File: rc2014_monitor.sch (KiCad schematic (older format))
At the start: 28 parts, among them J1 Z80 Bus, J2 Pro Bus, J3 USB_B_Micro, J4 M3 Mounting Hole, SW2 SW_Push, U1 74HCT541, U11 74HCT00, U2 74HCT541, U3 74HCT541, U7 MAX40200AUK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

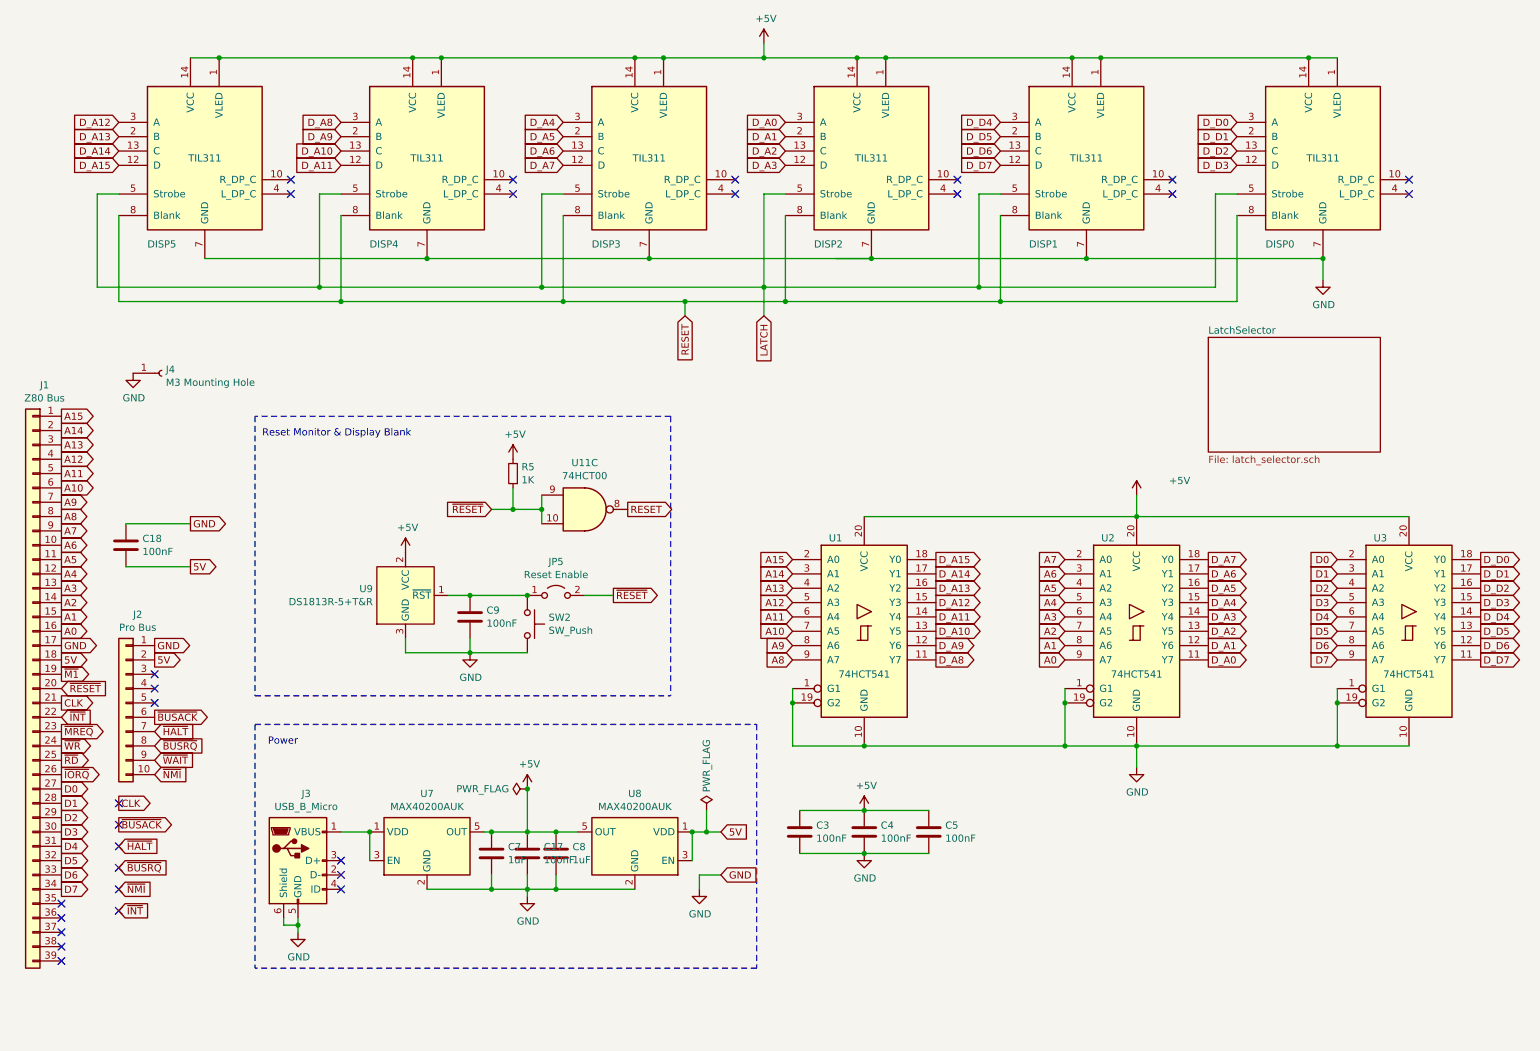
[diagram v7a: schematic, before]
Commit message: added extra filter cap, opened groundplane
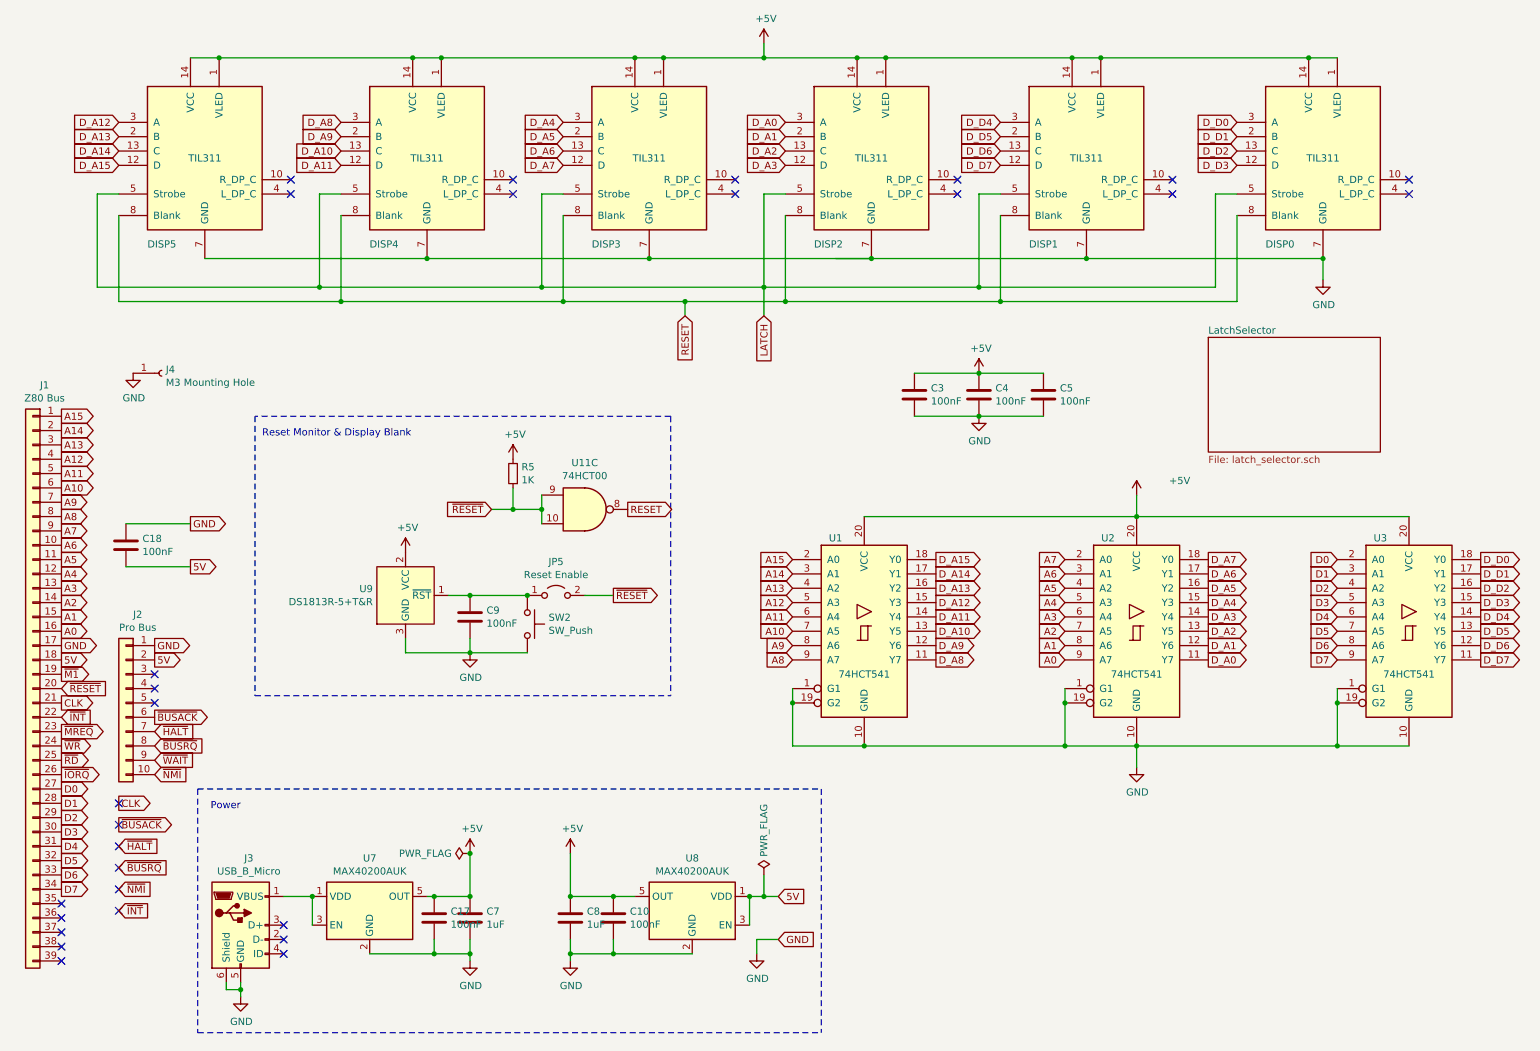
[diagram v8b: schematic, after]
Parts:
- added C10: 100nF, Capacitor_SMD:C_0805_2012Metric_Pad1.15x1.40mm_HandSolder, symbol Device:C
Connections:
- net +5V: now also C10.1
- net GND: now also C10.2
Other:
- moved on the sheet: C17, C3, C4, C5, C7, J3, U7, U8
